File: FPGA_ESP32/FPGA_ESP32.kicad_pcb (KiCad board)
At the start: 2 copper layers, 30.5 x 49.5 mm, 84 parts, among them J1 USB_Micro, J10 UART, J2 PWM, J3 CAM, J4 I2C, J5 U.FL-R-SMT(01), J7 Micro_SD_Card_Det, J9 I2C, U1 V3S, U2 ADP322ACPZ-145-R7, U3 MPU-9250_Obsolete, U5 ESP32-PICO-D4, U6 LT1963AxST-3.3, U7 BMP280, Y1 X1E0000210832, Y2 CC5V-T1A 32.768KHZ +-20PPM 12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

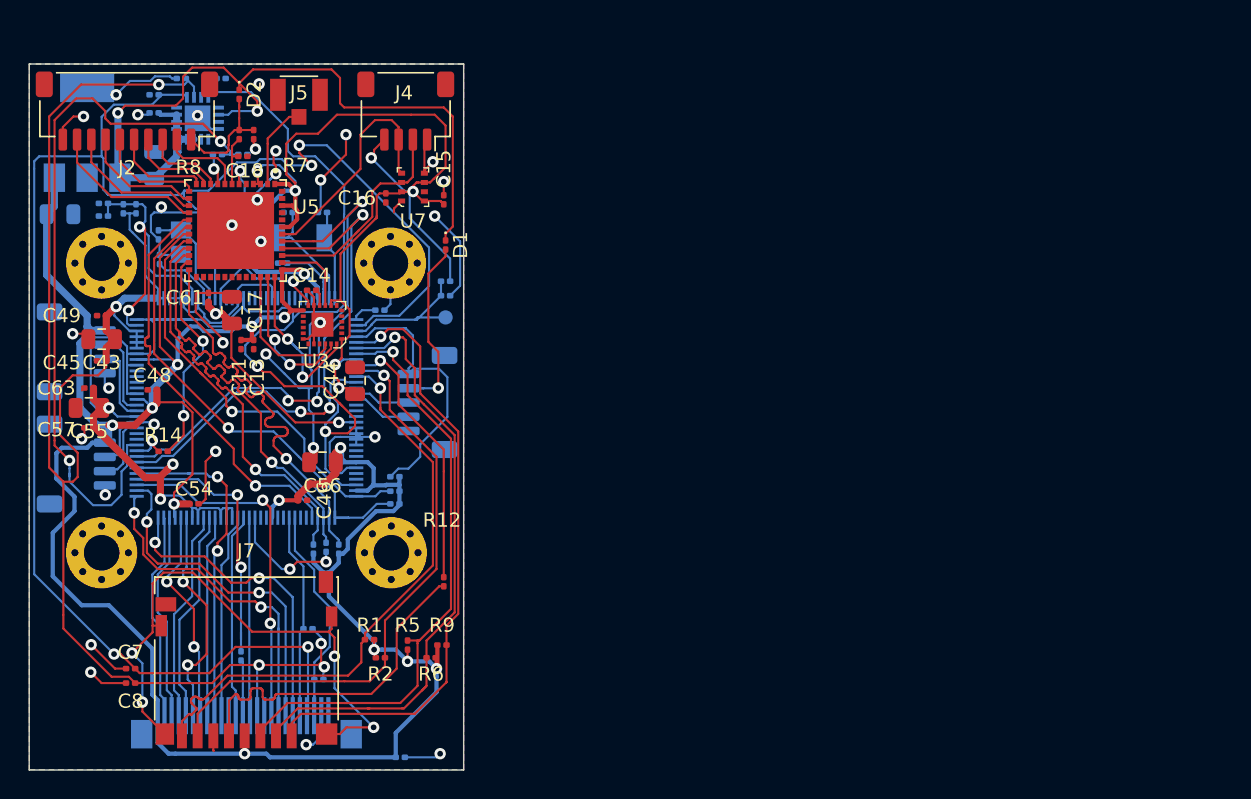
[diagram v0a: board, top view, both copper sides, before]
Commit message: FPGA_ESP32 : add header + esp32 with SDIO
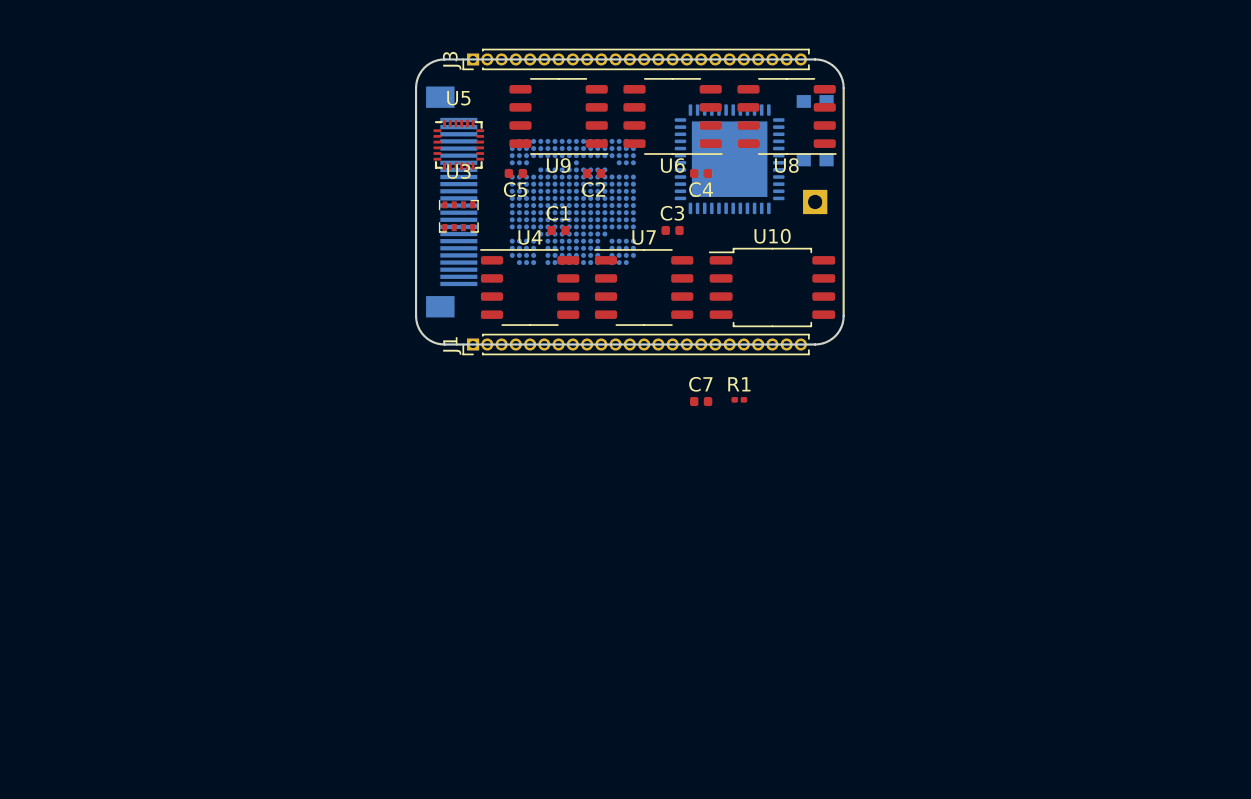
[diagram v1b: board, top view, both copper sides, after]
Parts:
- removed C10, C11, C38, C45, C46, C57, C6: 1uF, Capacitor_SMD:C_0201_0603Metric
- removed C12, C13, C14, C15, C16, C18, C48, C49, C54, C61, C63, C64, C65: 0.1uF, Capacitor_SMD:C_0201_0603Metric
- removed C17, C43, C44, C55, C56, C9: 10uF, Capacitor_SMD:C_0805_2012Metric
- removed C36, C37: 18pF, Capacitor_SMD:C_0201_0603Metric
- removed C40, C41: 20pF, Capacitor_SMD:C_0201_0603Metric
- removed C8: 4.7uF, Capacitor_SMD:C_0201_0603Metric
- removed D1, D2: D, Diode_SMD:D_0201_0603Metric
- removed J10: UART, Connector_JST:JST_SH_SM04B-SRSS-TB_1x04-1MP_P1.00mm_Horizontal
- removed J4, J9: I2C, Connector_JST:JST_SH_SM04B-SRSS-TB_1x04-1MP_P1.00mm_Horizontal
- removed J5: U.FL-R-SMT(01), U.FL-R-SMT_01_:HRS_U.FL-R-SMT(01)
- removed J7: Micro_SD_Card_Det, Connector_Card:microSD_HC_Hirose_DM3D-SF
- removed MH1, MH2, MH3, MH4: MountingHole_Pad, MountingHole:MountingHole_2.5mm_Pad_Via
- removed R10, R11, R29, R31, R32: 2K 1%, Resistor_SMD:R_0201_0603Metric
- removed R12, R17: 33R, Resistor_SMD:R_0201_0603Metric
- removed R13, R14, R15, R16, R18, R19, R2, R21, R3, R5, R6, R7, R8, R9: 47K, Resistor_SMD:R_0201_0603Metric
- removed R30: 6K 1%, Resistor_SMD:R_0201_0603Metric
- removed R4: 240R 1%, Resistor_SMD:R_0201_0603Metric
- removed TP4: CPU_RST, TestPoint:TestPoint_Pad_D1.0mm
- removed Y1: X1E0000210832, Crystal:Crystal_SMD_3225-4Pin_3.2x2.5mm
- removed Y2: CC5V-T1A 32.768KHZ +-20PPM 12.5PF, CC5V-T1A:SOIC-2
- added SW1: SW_Push, Button_Switch_SMD:SW_Push_1P1T_NO_CK_KMR2, B.Cu at (78.0, 25.0)
- added TP1: TestPoint, Connector_PinHeader_2.54mm:PinHeader_1x01_P2.54mm_Vertical, B.Cu at (78.0, 30.0)
- added U10: W25Q128JVS, Package_SO:SOIC-8_5.23x5.23mm_P1.27mm, F.Cu at (75.0, 36.0)
- added U4: LY68L6400SLIT, Package_SO:SSOP-8_3.9x5.05mm_P1.27mm, F.Cu at (58.0, 36.0)
- added U8: LY68L6400SLIT, Package_SO:SSOP-8_3.9x5.05mm_P1.27mm, F.Cu at (76.0, 24.0)
- added U9: LY68L6400SLIT, Package_SO:SSOP-8_3.9x5.05mm_P1.27mm, F.Cu at (60.0, 24.0)
- C1: value 0.1uF -> 100nF; footprint Capacitor_SMD:C_0201_0603Metric -> Capacitor_SMD:C_0402_1005Metric; moved to F.Cu
- C2, C3: value 1uF -> 100nF; footprint Capacitor_SMD:C_0201_0603Metric -> Capacitor_SMD:C_0402_1005Metric; moved to F.Cu
- C4: value 4.7uF -> 100nF; footprint Capacitor_SMD:C_0201_0603Metric -> Capacitor_SMD:C_0402_1005Metric; moved to F.Cu
- C5: value 10uF -> 100nF; footprint Capacitor_SMD:C_0805_2012Metric -> Capacitor_SMD:C_0402_1005Metric; moved to F.Cu
- C7: value 4.7uF -> 10nF; footprint Capacitor_SMD:C_0201_0603Metric -> Capacitor_SMD:C_0402_1005Metric
- J1: value USB_Micro -> Conn_01x24_Female; footprint Connector_JST:JST_SH_BM05B-SRSS-TB_1x05-1MP_P1.00mm_Vertical -> Connector_PinHeader_1.00mm:PinHeader_1x24_P1.00mm_Vertical; moved to F.Cu
- J2: value PWM -> CAM; footprint Connector_JST:JST_SH_SM10B-SRSS-TB_1x10-1MP_P1.00mm_Horizontal -> fpc_cam24:FPC_24_CAM; moved to B.Cu
- J3: value CAM -> Conn_01x24_Female; footprint fpc_cam24:FPC_24_CAM -> Connector_PinHeader_1.00mm:PinHeader_1x24_P1.00mm_Vertical; moved to F.Cu
- R1: value 47K -> 1K
- U1: value V3S -> LFE5UM-25F-7MG285C; footprint V3s:LQFP-128_14x14mm_P0.4mm -> footprints:BGA285N50P18X18_1000X1000X130N
- U2: value ADP322ACPZ-145-R7 -> ESP32-PICO-D4; footprint QFN50P300X300X90-17N:QFN50P300X300X90-17N -> Package_DFN_QFN:QFN-48-1EP_7x7mm_P0.5mm_EP5.3x5.3mm
- U3: value MPU-9250_Obsolete -> BMP280; footprint digikey-footprints:QFN-24-1EP_3x3mm -> Package_LGA:Bosch_LGA-8_2x2.5mm_P0.65mm_ClockwisePinNumbering
- U5: value ESP32-PICO-D4 -> ICM-20948; footprint ESP32-PICO-D4:PQFN50P700X700X104-49N -> Sensor_Motion:InvenSense_QFN-24_3x3mm_P0.4mm
- U6: value LT1963AxST-3.3 -> LY68L6400SLIT; footprint Package_TO_SOT_SMD:SOT-223-3_TabPin2 -> Package_SO:SSOP-8_3.9x5.05mm_P1.27mm; moved to F.Cu
- U7: value BMP280 -> LY68L6400SLIT; footprint digikey-footprints:LGA-8_2x2.5mm_BMP280 -> Package_SO:SSOP-8_3.9x5.05mm_P1.27mm
- moved J3 48.7 mm to (54.0, 20.0), turned to 90 degrees
- moved C7 44.2 mm to (70.0, 44.0), turned to 0 degrees
- moved U6 41.1 mm to (68.0, 24.0), turned to 180 degrees
- moved C1 38.6 mm to (60.0, 32.0)
- moved U2 37.4 mm to (72.0, 27.0)
- moved C3 33.4 mm to (68.0, 32.0)
- moved C2 31.2 mm to (62.5, 28.0)
- moved R1 30.9 mm to (72.7, 43.9), turned to 0 degrees
- moved U1 27.1 mm to (61.0, 30.0), turned to 0 degrees
- moved C5 25.4 mm to (57.0, 28.0), turned to 180 degrees
- moved C4 24.5 mm to (70.0, 28.0)
- moved J2 24.1 mm to (53.0, 30.0), turned to 90 degrees
- moved U7 17.7 mm to (66.0, 36.0), turned to 0 degrees
- moved U5 16.8 mm to (53.0, 26.0), turned to 0 degrees
- moved U3 12.2 mm to (53.0, 31.0), turned to 0 degrees
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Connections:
- C1 pad 1: +3V3 -> VIO
- C2 pad 1: /PMIC Power Battery/VIN -> VIO
- C3 pad 1: +1V2 -> VIO
- C4 pad 1: GND -> VIO
- C4 pad 2: Net-(C4-Pad2) -> GND
- C5 pad 1: /PMIC Power Battery/VIN -> VIO
- C7 pad 1: +3V0 -> /FPGA/ADCREF
- J1 pad 1: GND -> Net-(J1-Pad1)
- J1 pad 2: /USB_D_P -> Net-(J1-Pad2)
- J1 pad 3: /USB_D_N -> Net-(J1-Pad3)
- J1 pad 4: VBUS -> Net-(J1-Pad4)
- J1 pad 5: /USB_ID -> Net-(J1-Pad5)
- J2 pad 1: +BATT -> /FPGA/STROBE
- J2 pad 10: GND -> Net-(J2-Pad10)
- J2 pad 2: /WIFI, BT, RT/SENSOR_VN -> Net-(J2-Pad2)
- J2 pad 3: /WIFI, BT, RT/IO34 -> /FPGA/CSI_I2C_SDA
- J2 pad 4: /WIFI, BT, RT/IO35 -> /FPGA/CAM_AVDD
- J2 pad 5: /WIFI, BT, RT/IO32 -> /FPGA/CSI_I2C_SCL
- J2 pad 6: /WIFI, BT, RT/IO33 -> /FPGA/~CSI_RST
- J2 pad 7: /WIFI, BT, RT/IO25 -> /FPGA/CSI_VSYNC
- J2 pad 8: /WIFI, BT, RT/IO26 -> /FPGA/CSI_PWDN
- J2 pad 9: /WIFI, BT, RT/IO27 -> /FPGA/CSI_HSYNC
- J3 pad 1: (no net) -> Net-(J3-Pad1)
- J3 pad 10: (no net) -> Net-(J3-Pad10)
- J3 pad 11: +1V8 -> Net-(J3-Pad11)
- J3 pad 12: /All V3s input output/CSI_Y9 -> Net-(J3-Pad12)
- J3 pad 14: /All V3s input output/CSI_Y8 -> Net-(J3-Pad14)
- J3 pad 15: GND -> Net-(J3-Pad15)
- J3 pad 16: /All V3s input output/CSI_Y7 -> Net-(J3-Pad16)
- J3 pad 17: /All V3s input output/CSI_PCLK -> Net-(J3-Pad17)
- J3 pad 18: /All V3s input output/CSI_Y6 -> Net-(J3-Pad18)
- J3 pad 19: /All V3s input output/CSI_Y2 -> Net-(J3-Pad19)
- J3 pad 2: GND -> Net-(J3-Pad2)
- J3 pad 20: /All V3s input output/CSI_Y3 -> Net-(J3-Pad20)
- J3 pad 21: /All V3s input output/CSI_Y5 -> Net-(J3-Pad21)
- J3 pad 22: /All V3s input output/CSI_Y4 -> Net-(J3-Pad22)
- J3 pad 23: /All V3s input output/CSI_Y1 -> Net-(J3-Pad23)
- J3 pad 24: /All V3s input output/CSI_Y0 -> Net-(J3-Pad24)
- J3 pad 3: /All V3s input output/CSI_I2C_SDA -> Net-(J3-Pad3)
- J3 pad 4: +3V0 -> Net-(J3-Pad4)
- J3 pad 5: /All V3s input output/CSI_I2C_SCL -> Net-(J3-Pad5)
- J3 pad 6: /All V3s input output/~CSI_RST -> Net-(J3-Pad6)
- J3 pad 7: /All V3s input output/CSI_VSYNC -> Net-(J3-Pad7)
- J3 pad 8: /All V3s input output/CSI_PWDN -> Net-(J3-Pad8)
- J3 pad 9: /All V3s input output/CSI_HSYNC -> Net-(J3-Pad9)
- R1 pad 1: +3V3 -> /FPGA/ADCREF
- R1 pad 2: /All V3s input output/PF0 -> /FPGA/ADCREFOUT
- U2 pad 1: /PMIC Power Battery/VIN -> Net-(U2-Pad1)
- U2 pad 10: /PMIC Power Battery/VIN -> Net-(U2-Pad10)
- U2 pad 11: (no net) -> Net-(U2-Pad11)
- U2 pad 12: GND -> Net-(U2-Pad12)
- U2 pad 13: (no net) -> Net-(U2-Pad13)
- U2 pad 14: (no net) -> Net-(U2-Pad14)
- U2 pad 15: /PMIC Power Battery/VIN -> Net-(U2-Pad15)
- U2 pad 16: /PMIC Power Battery/VIN -> Net-(U2-Pad16)
- U2 pad 17: GND -> Net-(U2-Pad17)
- U2 pad 2: /PMIC Power Battery/VIN -> Net-(U2-Pad2)
- U2 pad 3: /PMIC Power Battery/VIN -> Net-(U2-Pad3)
- U2 pad 4: (no net) -> Net-(U2-Pad3)
- U2 pad 5: +3V0 -> Net-(U2-Pad5)
- U2 pad 6: +1V8 -> Net-(U2-Pad6)
- U2 pad 7: (no net) -> Net-(U2-Pad7)
- U2 pad 8: +1V2 -> Net-(U2-Pad8)
- U2 pad 9: (no net) -> Net-(U2-Pad9)
- U3 pad 1: +3V3 -> Net-(U3-Pad1)
- U3 pad 2: (no net) -> Net-(U3-Pad2)
- U3 pad 3: (no net) -> Net-(U3-Pad3)
- U3 pad 4: (no net) -> Net-(U3-Pad4)
- U3 pad 5: (no net) -> Net-(U3-Pad5)
- U3 pad 6: (no net) -> Net-(U3-Pad6)
- U3 pad 7: (no net) -> Net-(U3-Pad7)
- U3 pad 8: +3V3 -> Net-(U3-Pad8)
- U5 pad 1: +3V3 -> Net-(U5-Pad1)
- U5 pad 10: /WIFI, BT, RT/IO34 -> Net-(U5-Pad10)
- U5 pad 11: /WIFI, BT, RT/IO35 -> Net-(U5-Pad11)
- U5 pad 12: /WIFI, BT, RT/IO32 -> Net-(U5-Pad12)
- U5 pad 13: /WIFI, BT, RT/IO33 -> Net-(U5-Pad13)
- U5 pad 14: /WIFI, BT, RT/IO25 -> Net-(U5-Pad14)
- U5 pad 15: /WIFI, BT, RT/IO26 -> Net-(U5-Pad15)
- U5 pad 16: /WIFI, BT, RT/IO27 -> Net-(U5-Pad16)
- U5 pad 17: /All V3s input output/SDIO1_CLK -> Net-(U5-Pad17)
- U5 pad 18: /All V3s input output/SDIO1_DAT2 -> Net-(U5-Pad18)
- U5 pad 19: +3V3 -> Net-(U5-Pad19)
- U5 pad 20: /All V3s input output/SDIO1_DAT3 -> Net-(U5-Pad18)
- U5 pad 21: /All V3s input output/SDIO1_CMD -> Net-(U5-Pad21)
- U5 pad 22: /All V3s input output/SDIO1_DAT0 -> Net-(U5-Pad22)
- U5 pad 23: /WIFI, BT, RT/IO0 -> Net-(U5-Pad23)
- U5 pad 24: /All V3s input output/SDIO1_DAT1 -> Net-(U5-Pad24)
- U5 pad 3: +3V3 -> Net-(U5-Pad3)
- U5 pad 4: +3V3 -> Net-(U5-Pad4)
- U5 pad 5: (no net) -> Net-(U5-Pad5)
- U5 pad 6: /WIFI, BT, RT/ICM_INT -> Net-(U5-Pad6)
- U5 pad 8: /WIFI, BT, RT/SENSOR_VN -> Net-(U5-Pad8)
- U6 pad 1: /PMIC Power Battery/VIN -> /FPGA/RAM1_CE
- U6 pad 2: GND -> /FPGA/RAM1_SIO1
- U6 pad 3: +3V3 -> /FPGA/RAM1_SIO3
- U7 pad 1: GND -> /FPGA/RAM2_CE
- U7 pad 2: +3V3 -> /FPGA/RAM2_SIO1
- U7 pad 3: /WIFI, BT, RT/SDA -> /FPGA/RAM2_SIO3
- U7 pad 4: /WIFI, BT, RT/SCL -> GND
- U7 pad 5: GND -> /FPGA/RAM2_SIO0
- U7 pad 6: +3V3 -> /FPGA/RAM2_SCLK
- U7 pad 7: GND -> /FPGA/RAM2_SIO4
- U7 pad 8: +3V3 -> VIO
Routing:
- net +3V3: track 293.1 -> 0.00 mm, vias 19 -> 0
- net +3V0: track 143.3 -> 0.00 mm, vias 6 -> 0
- net +1V8: track 123.3 -> 0.00 mm, vias 5 -> 0
- net +1V2: track 122.8 -> 0.00 mm, vias 5 -> 0
- net GND: track 114.6 -> 0.00 mm, vias 31 -> 0
- net /PMIC Power Battery/VIN: track 69.8 -> 0.00 mm, vias 2 -> 0
- net /WIFI, BT, RT/EN: track 51.3 -> 0.00 mm, vias 2 -> 0
- net /All V3s input output/PF5: track 43.5 -> 0.00 mm, vias 1 -> 0
- net /All V3s input output/PF3: track 43.2 -> 0.00 mm, vias 1 -> 0
- net /All V3s input output/PF4: track 43.2 -> 0.00 mm, vias 1 -> 0
- net /All V3s input output/PF1: track 41.7 -> 0.00 mm, vias 1 -> 0
- net /All V3s input output/PF0: track 41.4 -> 0.00 mm, vias 1 -> 0
- net Net-(J7-Pad11): track 39.8 -> 0.00 mm, vias 4 -> 0
- net /WIFI, BT, RT/UART0_RX: track 38.3 -> 0.00 mm, vias 3 -> 0
- net /WIFI, BT, RT/UART0_TX: track 37.7 -> 0.00 mm, vias 3 -> 0
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- removed copper zone on B.Cu, net GND
- removed copper zone on F.Cu, net GND
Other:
- board size 30.5 x 49.5 mm -> 30 x 20 mm
- board text removed: "SmartBridgeMicro V0.2 By Crylog"

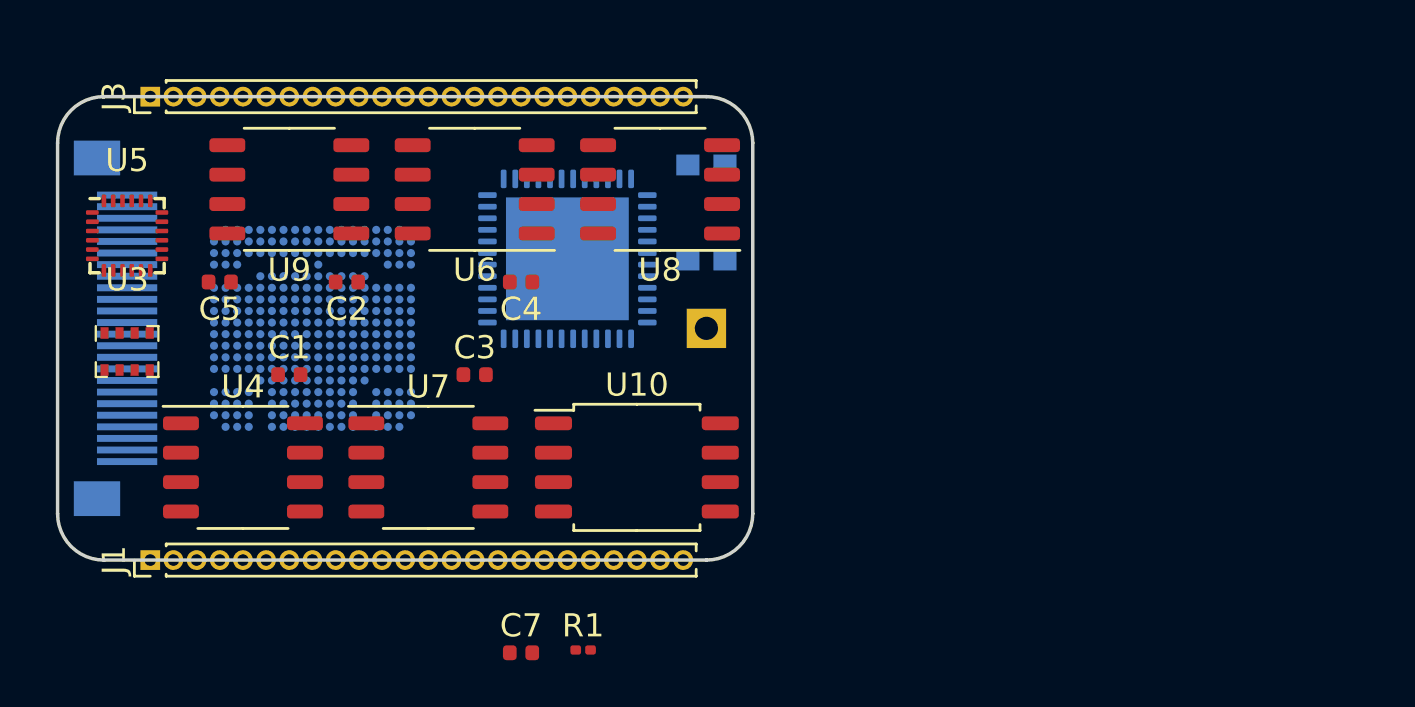
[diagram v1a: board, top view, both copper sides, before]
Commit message: FPGA_ESP32 : add 2 psram ic, rf switch
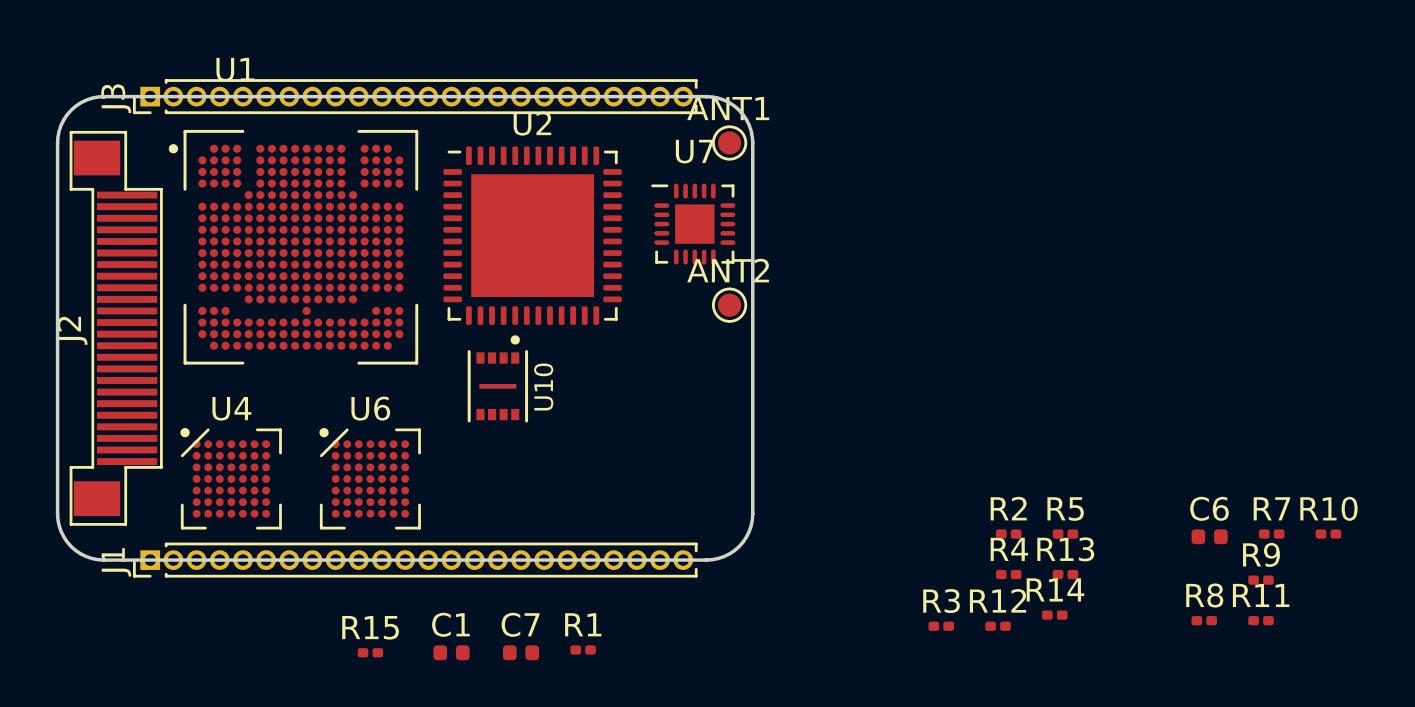
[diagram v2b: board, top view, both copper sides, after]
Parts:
- removed C2, C3, C4, C5: 100nF, Capacitor_SMD:C_0402_1005Metric
- removed SW1: SW_Push, Button_Switch_SMD:SW_Push_1P1T_NO_CK_KMR2
- removed U3: BMP280, Package_LGA:Bosch_LGA-8_2x2.5mm_P0.65mm_ClockwisePinNumbering
- removed U5: ICM-20948, Sensor_Motion:InvenSense_QFN-24_3x3mm_P0.4mm
- removed U8, U9: LY68L6400SLIT, Package_SO:SSOP-8_3.9x5.05mm_P1.27mm
- added ANT2: Antenna, TestPoint:TestPoint_Pad_D1.0mm, F.Cu at (79.0, 29.0)
- added C6: 100nF, Capacitor_SMD:C_0402_1005Metric, F.Cu at (99.7, 39.0)
- added R10: 4K7, Resistor_SMD:R_0201_0603Metric, F.Cu at (104.8, 38.9)
- added R11: 4K7, Resistor_SMD:R_0201_0603Metric, F.Cu at (101.9, 42.6)
- added R12: 4K7, Resistor_SMD:R_0201_0603Metric, F.Cu at (90.6, 42.9)
- added R13: 4K7, Resistor_SMD:R_0201_0603Metric, F.Cu at (93.5, 40.6)
- added R14: 4K7, Resistor_SMD:R_0201_0603Metric, F.Cu at (93.0, 42.4)
- added R15: R, Resistor_SMD:R_0201_0603Metric, F.Cu at (63.5, 44.0)
- added R2: 4K7, Resistor_SMD:R_0201_0603Metric, F.Cu at (91.0, 38.9)
- added R3: 4K7, Resistor_SMD:R_0201_0603Metric, F.Cu at (88.1, 42.9)
- added R4: 4K7, Resistor_SMD:R_0201_0603Metric, F.Cu at (91.0, 40.6)
- added R5: 4K7, Resistor_SMD:R_0201_0603Metric, F.Cu at (93.5, 38.9)
- added R7: 4K7, Resistor_SMD:R_0201_0603Metric, F.Cu at (102.4, 38.9)
- added R8: 4K7, Resistor_SMD:R_0201_0603Metric, F.Cu at (99.5, 42.6)
- added R9: 4K7, Resistor_SMD:R_0201_0603Metric, F.Cu at (101.9, 40.9)
- ANT1: renamed from TP1; value TestPoint -> Antenna; footprint Connector_PinHeader_2.54mm:PinHeader_1x01_P2.54mm_Vertical -> TestPoint:TestPoint_Pad_D1.0mm; moved to F.Cu
- J2, U1, U2: moved to F.Cu
- U10: value W25Q128JVS -> GD25Q16CEIGR; footprint Package_SO:SOIC-8_5.23x5.23mm_P1.27mm -> footprints:PSON50P200X300X50-9N
- U4, U6: value LY68L6400SLIT -> W956D6KBKX; footprint Package_SO:SSOP-8_3.9x5.05mm_P1.27mm -> footprints:BGA-49_7x7_4.0x4.0mm
- U7: value LY68L6400SLIT -> RFX2411; footprint Package_SO:SSOP-8_3.9x5.05mm_P1.27mm -> footprints:QFN-20_EP_3x3_Pitch0.4mm
- moved U7 15.6 mm to (77.5, 25.5)
- moved C1 13.9 mm to (67.0, 44.0)
- moved U6 13.3 mm to (63.5, 36.5), turned to 0 degrees
- moved ANT1 8.06 mm to (79.0, 22.0)
- moved U10 6.95 mm to (69.0, 32.5), turned to 270 degrees
- moved U1 3.54 mm to (60.5, 26.5)
- moved U2 1.80 mm to (70.5, 26.0)
- moved U4 0.71 mm to (57.5, 36.5)
- turned J2 to 270 degrees
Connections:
- net /FPGA/CSI_Y0 renamed Net-(J2-Pad24)
- net /FPGA/CSI_Y1 renamed Net-(J2-Pad23)
- net /FPGA/STROBE renamed Net-(J2-Pad1)
- net Net-(U1-PadA8) renamed /FPGA/RAM2_ADQ13
- net Net-(U1-PadA9) renamed /FPGA/RAM2_ADQ12
- net Net-(U1-PadB8) renamed /FPGA/RAM2_ADQ8
- net Net-(U1-PadB9) renamed /FPGA/RAM2_ADQ10
- net Net-(U1-PadC8) renamed /FPGA/RAM2_ADQ9
- net Net-(U1-PadC9) renamed /FPGA/RAM2_ADQ11
- C1 pad 1: VIO -> Net-(C1-Pad1)
- C1 pad 2: GND -> Net-(C1-Pad2)
- J1 pad 1: Net-(J1-Pad1) -> VIO
- J1 pad 10: Net-(J1-Pad10) -> IO4
- J1 pad 11: Net-(J1-Pad11) -> IO5
- J1 pad 12: Net-(J1-Pad12) -> IO6
- J1 pad 13: Net-(J1-Pad13) -> IO7
- J1 pad 14: Net-(J1-Pad14) -> IO8
- J1 pad 15: Net-(J1-Pad15) -> IO9
- J1 pad 16: Net-(J1-Pad16) -> IO10
- J1 pad 17: Net-(J1-Pad17) -> IO11
- J1 pad 18: Net-(J1-Pad18) -> IO12
- J1 pad 19: Net-(J1-Pad19) -> IO13
- J1 pad 2: Net-(J1-Pad2) -> +1V8
- J1 pad 20: Net-(J1-Pad20) -> IO14
- J1 pad 21: Net-(J1-Pad21) -> IO15
- J1 pad 22: Net-(J1-Pad22) -> IO16
- J1 pad 23: Net-(J1-Pad23) -> IO17
- J1 pad 24: Net-(J1-Pad24) -> IO18
- J1 pad 3: Net-(J1-Pad3) -> +2V8
- J1 pad 4: Net-(J1-Pad4) -> GND
- J1 pad 5: Net-(J1-Pad5) -> VIN
- J1 pad 6: Net-(J1-Pad6) -> IO0
- J1 pad 7: Net-(J1-Pad7) -> IO1
- J1 pad 8: Net-(J1-Pad8) -> IO2
- J1 pad 9: Net-(J1-Pad9) -> IO3
- J2 pad 11: /FPGA/CAM_DOVDD -> +1V8
- J2 pad 15: Net-(J2-Pad15) -> GND
- J2 pad 2: Net-(J2-Pad2) -> GND
- J2 pad 3: /FPGA/CSI_I2C_SDA -> IO27
- J2 pad 4: /FPGA/CAM_AVDD -> +2V8
- J2 pad 5: /FPGA/CSI_I2C_SCL -> IO28
- J3 pad 1: Net-(J3-Pad1) -> VIO
- J3 pad 10: Net-(J3-Pad10) -> IO23
- J3 pad 11: Net-(J3-Pad11) -> IO24
- J3 pad 12: Net-(J3-Pad12) -> IO25
- J3 pad 13: Net-(J3-Pad13) -> IO26
- J3 pad 14: Net-(J3-Pad14) -> IO27
- J3 pad 15: Net-(J3-Pad15) -> IO28
- J3 pad 16: Net-(J3-Pad16) -> IO29
- J3 pad 17: Net-(J3-Pad17) -> IO30
- J3 pad 18: Net-(J3-Pad18) -> IO31
- J3 pad 19: Net-(J3-Pad19) -> IO32
- J3 pad 2: Net-(J3-Pad2) -> +1V8
- J3 pad 20: Net-(J3-Pad20) -> IO33
- J3 pad 21: Net-(J3-Pad21) -> IO34
- J3 pad 22: Net-(J3-Pad22) -> IO35
- J3 pad 23: Net-(J3-Pad23) -> IO36
- J3 pad 24: Net-(J3-Pad24) -> IO37
- J3 pad 3: Net-(J3-Pad3) -> +2V8
- J3 pad 4: Net-(J3-Pad4) -> GND
- J3 pad 5: Net-(J3-Pad5) -> VIN
- J3 pad 6: Net-(J3-Pad6) -> IO19
- J3 pad 7: Net-(J3-Pad7) -> IO20
- J3 pad 8: Net-(J3-Pad8) -> IO21
- J3 pad 9: Net-(J3-Pad9) -> IO22
- U1 pad A10: Net-(U1-PadA10) -> /FPGA/SDIO1_DAT1
- U1 pad A11: Net-(U1-PadA11) -> /FPGA/SDIO1_DAT0
- U1 pad A12: Net-(U1-PadA12) -> /FPGA/CSI_Y9
- U1 pad A13: Net-(U1-PadA13) -> /FPGA/~CSI_RST
- U1 pad A15: Net-(U1-PadA15) -> /FPGA/CSI_VSYNC
- U1 pad A16: Net-(U1-PadA16) -> /FPGA/CSI_MCLK
- U1 pad A17: Net-(U1-PadA17) -> IO27
- U1 pad A2: Net-(U1-PadA2) -> /FPGA/RAM1_A16
- U1 pad A3: Net-(U1-PadA3) -> /FPGA/RAM1_ADQ14
- U1 pad A4: /FPGA/RAM4_SCLK -> /FPGA/RAM1_ADQ5
- U1 pad A6: /FPGA/RAM4_CE -> /FPGA/RAM1_ADQ4
- U1 pad A7: /FPGA/RAM4_SIO1 -> /FPGA/RAM1_ADQ7
- U1 pad B1: Net-(U1-PadB1) -> /FPGA/RAM1_A18
- U1 pad B10: Net-(U1-PadB10) -> /FPGA/SDIO1_DAT2
- U1 pad B11: Net-(U1-PadB11) -> /FPGA/SDIO1_CLK
- U1 pad B12: Net-(U1-PadB12) -> /FPGA/CSI_Y7
- U1 pad B13: Net-(U1-PadB13) -> /FPGA/CSI_Y2
- U1 pad B15: Net-(U1-PadB15) -> /FPGA/CSI_HSYNC
- U1 pad B17: Net-(U1-PadB17) -> IO28
- U1 pad B18: Net-(U1-PadB18) -> IO29
- U1 pad B2: Net-(U1-PadB2) -> /FPGA/RAM1_ADQ15
- U1 pad B6: /FPGA/RAM4_SIO0 -> /FPGA/RAM1_ADQ6
- U1 pad B7: Net-(U1-PadB7) -> /FPGA/RAM1_ADQ11
- U1 pad C1: Net-(U1-PadC1) -> /FPGA/RAM1_A19
- U1 pad C10: Net-(U1-PadC10) -> /FPGA/SDIO1_DAT3
- U1 pad C11: Net-(U1-PadC11) -> /FPGA/SDIO1_CMD
- U1 pad C12: Net-(U1-PadC12) -> /FPGA/CSI_Y8
- U1 pad C13: Net-(U1-PadC13) -> /FPGA/CSI_Y5
- U1 pad C15: Net-(U1-PadC15) -> /FPGA/CSI_PWDN
- U1 pad C16: Net-(U1-PadC16) -> /FPGA/CSI_PCLK
- U1 pad C17: Net-(U1-PadC17) -> IO30
- U1 pad C18: /FPGA/RAM2_SIO1 -> /FPGA/RAM0_ADQ15
- U1 pad C2: Net-(U1-PadC2) -> /FPGA/RAM1_ADQ13
- U1 pad C4: Net-(U1-PadC4) -> /FPGA/ADCREFOUT
- U1 pad C6: /FPGA/RAM4_SIO4 -> /FPGA/RAM1_ADQ9
- U1 pad C7: Net-(U1-PadC7) -> /FPGA/RAM1_ADQ10
- U1 pad D1: Net-(U1-PadD1) -> /FPGA/RAM1_A20
- U1 pad D12: Net-(U1-PadD12) -> VIO
- U1 pad D13: Net-(U1-PadD13) -> /FPGA/CSI_Y6
- U1 pad D15: Net-(U1-PadD15) -> /FPGA/CSI_Y4
- U1 pad D16: Net-(U1-PadD16) -> /FPGA/CSI_Y3
- U1 pad D17: /FPGA/RAM2_SIO0 -> /FPGA/RAM0_ADQ14
- U1 pad D18: /FPGA/RAM2_SIO3 -> /FPGA/RAM0_A16
- U1 pad D2: Net-(U1-PadD2) -> /FPGA/RAM1_A17
- U1 pad D3: Net-(U1-PadD3) -> /FPGA/RAM1_ADQ12
- U1 pad D4: Net-(U1-PadD4) -> /FPGA/RAM1_A21
- U1 pad D6: /FPGA/RAM4_SIO3 -> /FPGA/RAM1_ADQ8
- U1 pad D7: Net-(U1-PadD7) -> VIO
- U1 pad F1: Net-(U1-PadF1) -> IO21
- U1 pad F15: /FPGA/RAM3_SIO0 -> /FPGA/RAM0_A20
- U1 pad F16: /FPGA/RAM3_SCLK -> /FPGA/RAM0_A19
- U1 pad F17: /FPGA/RAM3_CE -> /FPGA/RAM0_A18
- U1 pad F18: /FPGA/RAM2_SIO4 -> /FPGA/RAM0_A17
- U1 pad F2: Net-(U1-PadF2) -> IO0
- U1 pad G1: Net-(U1-PadG1) -> IO1
- U1 pad G14: VIO -> +1V8
- U1 pad G15: /FPGA/RAM0_SIO0 -> /FPGA/RAM0_ADQ2
- U1 pad G16: /FPGA/RAM3_SIO1 -> /FPGA/RAM0_A21
- U1 pad G18: /FPGA/RAM0_CE -> /FPGA/RAM0_ADQ0
- U1 pad G3: Net-(U1-PadG3) -> IO24
- U1 pad H1: Net-(U1-PadH1) -> IO22
- U1 pad H14: VIO -> +1V8
- U1 pad H15: /FPGA/RAM0_SIO1 -> /FPGA/RAM0_ADQ3
- U1 pad H16: /FPGA/RAM0_SIO3 -> /FPGA/RAM0_ADQ4
- U1 pad H17: /FPGA/RAM0_SCLK -> /FPGA/RAM0_ADQ1
- U1 pad H18: /FPGA/RAM3_SIO4 -> /FPGA/RAM1_ADQ1
- U1 pad H2: Net-(U1-PadH2) -> IO26
- U1 pad H3: Net-(U1-PadH3) -> IO23
- U1 pad J1: Net-(U1-PadJ1) -> IO20
- U1 pad J16: /FPGA/RAM0_SIO4 -> /FPGA/RAM0_ADQ5
- U1 pad J17: /FPGA/RAM3_SIO3 -> /FPGA/RAM1_ADQ0
- U1 pad J18: /FPGA/RAM1_CE -> /FPGA/RAM0_ADQ6
- U1 pad J2: Net-(U1-PadJ2) -> /FPGA/ADCREF
- U1 pad J3: Net-(U1-PadJ3) -> IO25
- U1 pad K1: Net-(U1-PadK1) -> IO5
- U1 pad K15: /FPGA/RAM1_SIO1 -> /FPGA/RAM0_ADQ9
- U1 pad K16: /FPGA/RAM1_SIO0 -> /FPGA/RAM0_ADQ8
- U1 pad K17: /FPGA/RAM1_SIO3 -> /FPGA/RAM0_ADQ10
- U1 pad K18: /FPGA/RAM1_SCLK -> /FPGA/RAM0_ADQ7
- U1 pad K2: Net-(U1-PadK2) -> IO10
- U1 pad K3: Net-(U1-PadK3) -> IO4
- U1 pad K4: Net-(U1-PadK4) -> IO6
- U1 pad L1: Net-(U1-PadL1) -> IO11
- U1 pad L15: /FPGA/RAM2_CE -> /FPGA/RAM0_ADQ12
- U1 pad L16: /FPGA/RAM2_SCLK -> /FPGA/RAM0_ADQ13
- U1 pad L18: /FPGA/RAM1_SIO4 -> /FPGA/RAM0_ADQ11
- U1 pad L3: Net-(U1-PadL3) -> IO3
- U1 pad L4: Net-(U1-PadL4) -> IO7
- U1 pad M16: Net-(U1-PadM16) -> /FPGA/RAM1_ADQ2
- U1 pad M17: Net-(U1-PadM17) -> /FPGA/RAM1_ADQ3
- U1 pad M2: Net-(U1-PadM2) -> IO12
- U1 pad M3: Net-(U1-PadM3) -> IO2
- U1 pad N2: Net-(U1-PadN2) -> IO19
- U1 pad N3: Net-(U1-PadN3) -> IO9
- U1 pad N4: Net-(U1-PadN4) -> IO8
- U1 pad T13: /FPGA/TDI -> IO36
- U1 pad T15: /FPGA/PROGRAMN -> /WIFI, BT, RT/FPGA_PROGRAMN
- U1 pad U13: /FPGA/TCK -> IO37
- U1 pad U14: Net-(U1-PadU14) -> GND
- U1 pad U16: /FPGA/FLASH_SCK -> /WIFI, BT, RT/FLASH_CLK
- U1 pad V13: /FPGA/TMS -> IO31
- U1 pad V14: /FPGA/TDO -> IO32
- U1 pad V15: Net-(U1-PadV15) -> GND
- U10 pad 1: Net-(U10-Pad1) -> /WIFI, BT, RT/CS
- U10 pad 2: Net-(U10-Pad2) -> /FPGA/FLASH_MISO
- U10 pad 3: Net-(U10-Pad3) -> /WIFI, BT, RT/WP
- U10 pad 4: Net-(U10-Pad4) -> GND
- U10 pad 5: Net-(U10-Pad5) -> /FPGA/FLASH_MOSI
- U10 pad 6: Net-(U10-Pad6) -> /WIFI, BT, RT/FLASH_CLK
- U10 pad 7: Net-(U10-Pad7) -> /WIFI, BT, RT/HOLD
- U10 pad 8: Net-(U10-Pad8) -> VIO
- U2 pad 11: Net-(U2-Pad11) -> IO17
- U2 pad 14: Net-(U2-Pad14) -> /WIFI, BT, RT/HOLD
- U2 pad 15: Net-(U2-Pad15) -> /WIFI, BT, RT/CS
- U2 pad 16: Net-(U2-Pad16) -> /WIFI, BT, RT/WP
- U2 pad 17: Net-(U2-Pad17) -> /FPGA/SDIO1_CLK
- U2 pad 18: Net-(U2-Pad18) -> /FPGA/SDIO1_DAT2
- U2 pad 20: Net-(U2-Pad20) -> /FPGA/SDIO1_DAT3
- U2 pad 21: Net-(U2-Pad21) -> /FPGA/SDIO1_CMD
- U2 pad 22: Net-(U2-Pad22) -> /FPGA/SDIO1_DAT0
- U2 pad 23: Net-(U2-Pad23) -> IO35
- U2 pad 24: Net-(U2-Pad24) -> /FPGA/SDIO1_DAT1
- U2 pad 28: Net-(U2-Pad28) -> IO15
- U2 pad 29: Net-(U2-Pad29) -> IO16
- U2 pad 34: Net-(U2-Pad34) -> /FPGA/INITN
- U2 pad 35: Net-(U2-Pad35) -> /WIFI, BT, RT/FLASH_CLK
- U2 pad 36: Net-(U2-Pad36) -> /FPGA/FLASH_MOSI
- U2 pad 38: Net-(U2-Pad38) -> /FPGA/FLASH_MISO
- U2 pad 39: Net-(U2-Pad39) -> /WIFI, BT, RT/IO2_PULL
- U2 pad 40: Net-(U2-Pad40) -> IO14
- U2 pad 41: Net-(U2-Pad41) -> IO13
- U2 pad 42: Net-(U2-Pad42) -> /WIFI, BT, RT/FPGA_PROGRAMN
- U2 pad 49: Net-(U2-Pad49) -> GND
- U2 pad 5: Net-(U2-Pad5) -> IO18
- U2 pad 6: Net-(U2-Pad6) -> /FPGA/DONE
- U2 pad 7: Net-(U2-Pad7) -> IO33
- U2 pad 8: Net-(U2-Pad8) -> IO34
- U7 pad 1: /FPGA/RAM2_CE -> Net-(U7-Pad1)
- U7 pad 2: /FPGA/RAM2_SIO1 -> Net-(U7-Pad2)
- U7 pad 3: /FPGA/RAM2_SIO3 -> Net-(U7-Pad3)
- U7 pad 4: GND -> Net-(U7-Pad4)
- U7 pad 5: /FPGA/RAM2_SIO0 -> Net-(U7-Pad5)
- U7 pad 6: /FPGA/RAM2_SCLK -> Net-(U7-Pad6)
- U7 pad 7: /FPGA/RAM2_SIO4 -> Net-(U7-Pad7)
- U7 pad 8: VIO -> Net-(U7-Pad8)

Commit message: FPGA_ESP32 : add spi mux
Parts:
- added U3: TMUX1574, footprints:QFP-16_1.85x2.65_Pitch0.4mm, F.Cu at (68.5, 33.0)
- moved U10 3.04 mm to (72.0, 33.0)
